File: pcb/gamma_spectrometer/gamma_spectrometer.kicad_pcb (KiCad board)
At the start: 4 copper layers, 45 x 45 mm, 184 parts, among them J101 DX07S024WJ3R400, Q201 IRLML0040, Q401 MMBTA42, Q402 MMBTA42, Q403 MMBTA42, T201 ATB322524-0110-T000, U101 LP5907MFX-3.3, U102 AMS1117-3.3, U103 FT231XQ, U104 TPS60400DBV, U201 max1847eee+, U202 TL431, U301 TL431, U302 STM32G474MET6, U303 W25Q64JVSSIQ, U401 AD8000YRDZ-REEL, Y301 ABM8G-16.000MHZ-4Y-T3

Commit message: pcb: рабочее состояние разводки USB/Power (промежуточное сохранение)
Co-Authored-By: Claude Opus 4.8 <noreply@anthropic.com>
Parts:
- C107, C109, U103: moved to B.Cu
- moved C106 73.5 mm to (113.5, 106.0)
- moved C103 72.3 mm to (111.0, 113.5)
- moved C108 71.9 mm to (113.5, 108.0)
- moved C105 71.9 mm to (112.5, 93.5), turned to 90 degrees
- moved C104 70.7 mm to (107.5, 106.5), turned to 180 degrees
- moved C107 67.3 mm to (111.9, 95.0)
- moved U102 63.1 mm to (112.0, 101.0)
- moved U101 62.5 mm to (113.5, 110.5)
- moved C101 59.0 mm to (92.5, 107.0), turned to 180 degrees
- moved C102 58.6 mm to (98.0, 105.0)
- moved C109 56.9 mm to (102.6, 92.5), turned to 180 degrees
- moved C110 55.6 mm to (98.0, 106.5)
- moved C112 55.0 mm to (92.5, 110.5), turned to 180 degrees
- moved C116 53.2 mm to (93.1, 117.0), turned to 180 degrees
- moved R101 52.9 mm to (106.5, 89.5), turned to 180 degrees
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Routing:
- net +5V_USB: track 0.00 -> 33.1 mm
- net +3.3V_D: track 0.00 -> 30.4 mm, vias 0 -> 2
- net Net-(F101-Pad1): track 0.00 -> 22.1 mm, vias 0 -> 2
- net +5V_A: track 0.00 -> 15.8 mm
- net /USB_Power_Board/D_N: track 0.00 -> 14.7 mm, vias 0 -> 3
- net GND: track 0.00 -> 13.7 mm, vias 0 -> 41
- net /USB_Power_Board/D_P: track 0.00 -> 11.9 mm, vias 0 -> 1
- net Net-(U104-OUT): track 0.00 -> 8.32 mm
- net Net-(U104-C_{FLY+}): track 0.00 -> 7.31 mm
- net −5V_A: track 0.00 -> 6.64 mm
- net +5V_HV: track 0.00 -> 5.53 mm
- net Net-(J101-PadB5): track 0.00 -> 4.36 mm
- net +3.3V_A: track 0.00 -> 3.74 mm
- net Net-(J101-PadA5): track 0.00 -> 3.09 mm
- net Net-(U103-CBUS0): track 0.00 -> 2.81 mm, vias 0 -> 1
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- added copper zone on B.Cu, net GND
- added copper zone on F.Cu, net GND
- added copper zone on In1.Cu, net GND

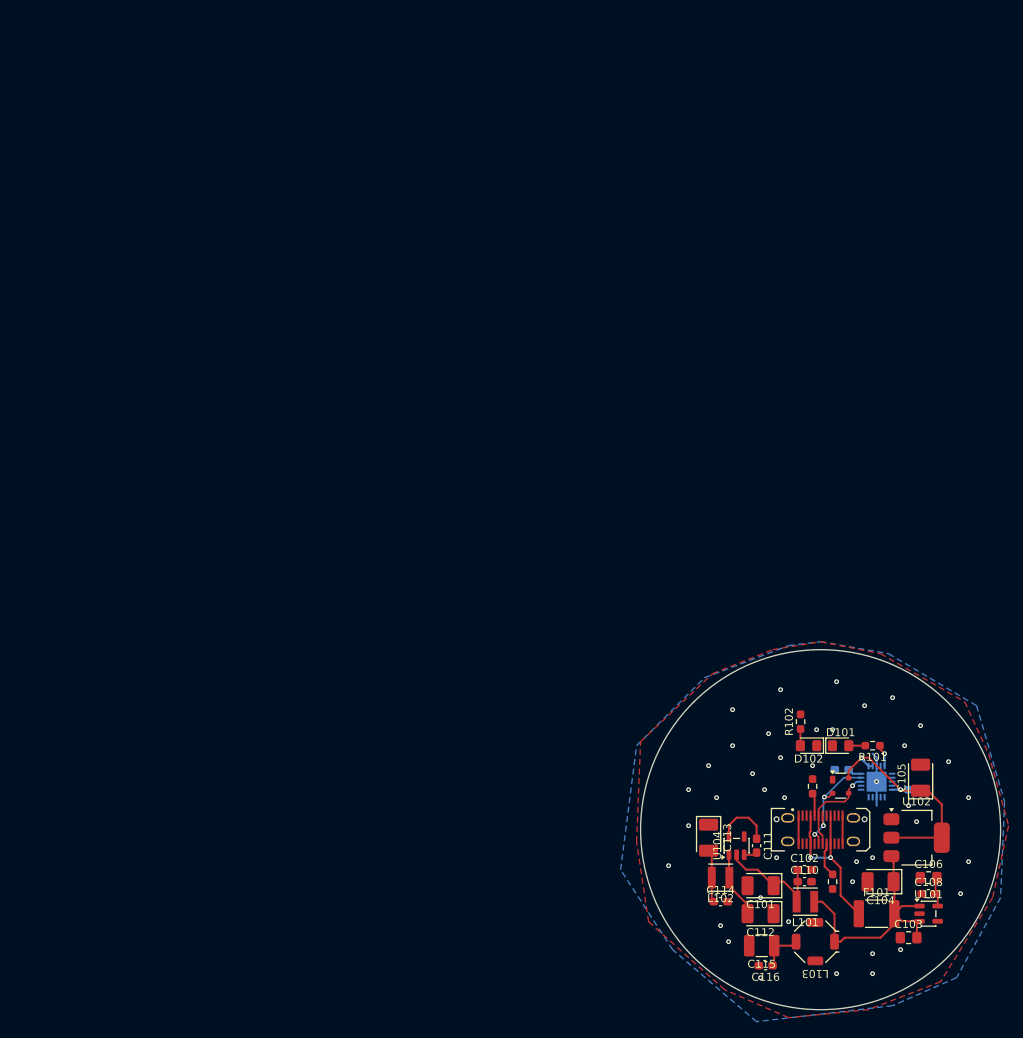
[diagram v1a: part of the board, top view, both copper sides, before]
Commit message: pcb(usb): односторонний монтаж + стойки M2.5 + своп ESD D+/D−
- FT231X (U103) + C107/C109 перенесены на верхний слой → на B.Cu
  компонентов 0, монтаж односторонний (проще/дешевле в сборке).
- U_ESD101: D+/D− переставлены на I/O1/I/O2 (пины симметричны по
  даташиту PRTR5V0U2X) ради компоновки; идентичность линий сохранена
  (D+ →USBDP, D− →USBDM). Нетлист переэкспортирован.
- Стойки M2.5 (STANDOFF_x3_TRIANGLE) в центр (100,100), все 3 пэда на GND.
- docs: usb_power_board_schematic синхронизирован (D+/D− таблица,
  корпус SOT143B вместо ошибочного SOT-363); добавлен даташит PRTR5V0U2X.

Co-Authored-By: Claude Opus 4.8 <noreply@anthropic.com>
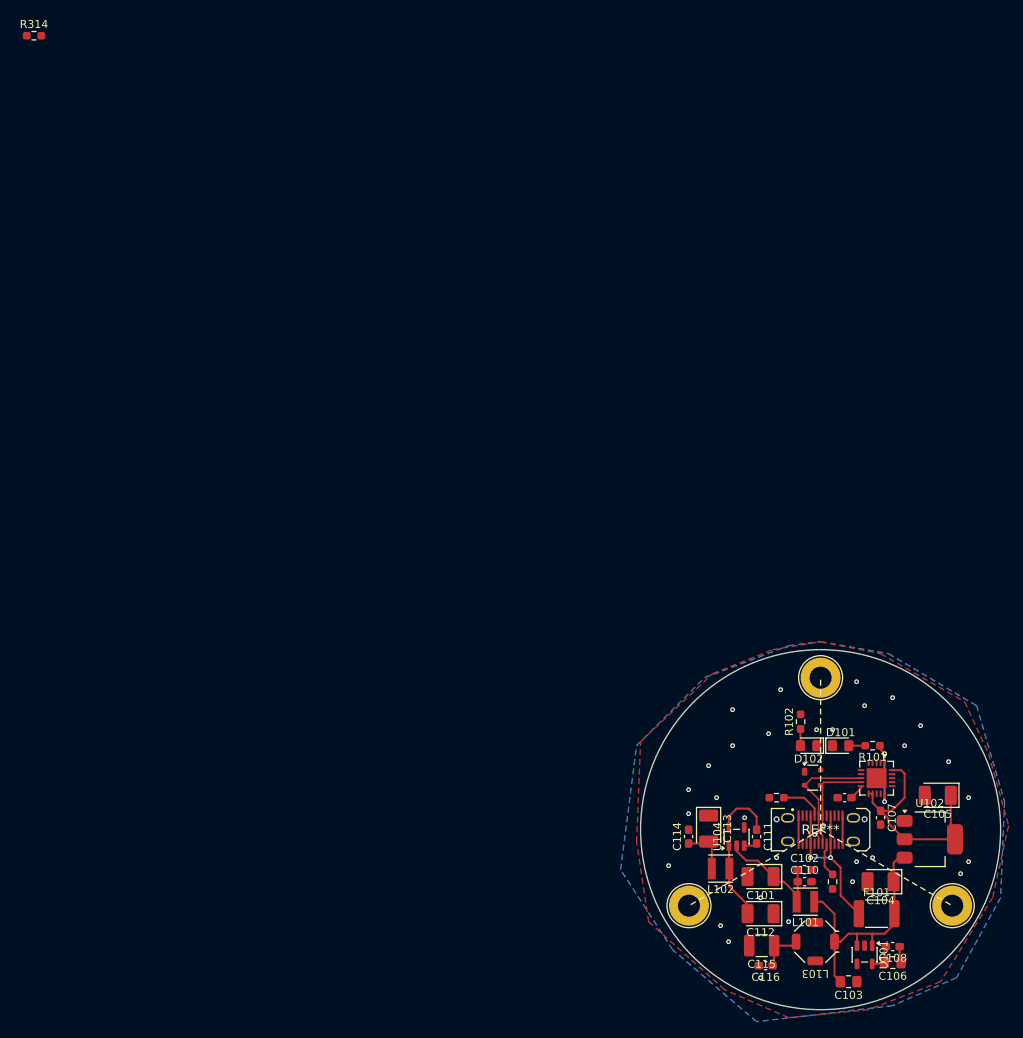
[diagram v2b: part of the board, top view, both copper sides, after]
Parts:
- added R314: 10k, Resistor_SMD:R_0603_1608Metric_Pad0.98x0.95mm_HandSolder, F.Cu at (1.68, 0.76)
- added REF**: STANDOFF_M2.5_GND_x3_TRIANGLE, посадочные места:STANDOFF_M2.5_GND_x3_TRIANGLE, F.Cu at (100.0, 100.0)
- C107, C109, U103: moved to F.Cu
- R412: value 499k -> 1M
- moved C106 11.5 mm to (109.0, 116.6), turned to 180 degrees
- moved U101 9.51 mm to (105.5, 115.6), turned to -90 degrees
- moved C103 9.30 mm to (103.5, 119.0), turned to 180 degrees
- moved C114 9.07 mm to (83.5, 100.9), turned to 90 degrees
- moved C108 7.99 mm to (109.0, 114.6), turned to 180 degrees
- moved C107 5.59 mm to (107.5, 98.5), turned to -90 degrees
- moved R_CC102 4.72 mm to (94.5, 96.0), turned to 180 degrees
- moved U_ESD101 3.64 mm to (99.0, 93.5)
- moved C109 3.52 mm to (103.0, 96.0)
- moved C105 3.08 mm to (114.7, 95.7), turned to 180 degrees
- moved U102 1.66 mm to (113.7, 101.2)
- moved C101 1.14 mm to (92.5, 105.9)
- moved C111 1.14 mm to (92.0, 100.9)
- moved C113 1.14 mm to (86.0, 99.9)
- moved L102 1.14 mm to (87.5, 104.9)
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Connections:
- Q403 pad 3: Net-(Q403-C) -> GND
- R412 pad 2: Net-(Q403-C) -> GND
- U_ESD101 pad 2: /USB_Power_Board/D_N -> /USB_Power_Board/D_P
- U_ESD101 pad 3: /USB_Power_Board/D_P -> /USB_Power_Board/D_N
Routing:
- net Net-(U103-CBUS0): track 2.81 -> 7.83 mm, vias 1 -> 2
- net GND: track 13.7 -> 9.07 mm, vias 41 -> 30
- net /USB_Power_Board/D_P: track 11.9 -> 15.7 mm, vias 1 -> 0
- net Net-(J101-PadA5): track 3.09 -> 5.32 mm
- net +3.3V_D: track 30.4 -> 28.3 mm, vias 2 -> 0
- net /USB_Power_Board/D_N: track 14.7 -> 13.4 mm, vias 3 -> 2
- net Net-(U104-OUT): track 8.32 -> 9.46 mm
- net −5V_A: track 6.64 -> 6.14 mm

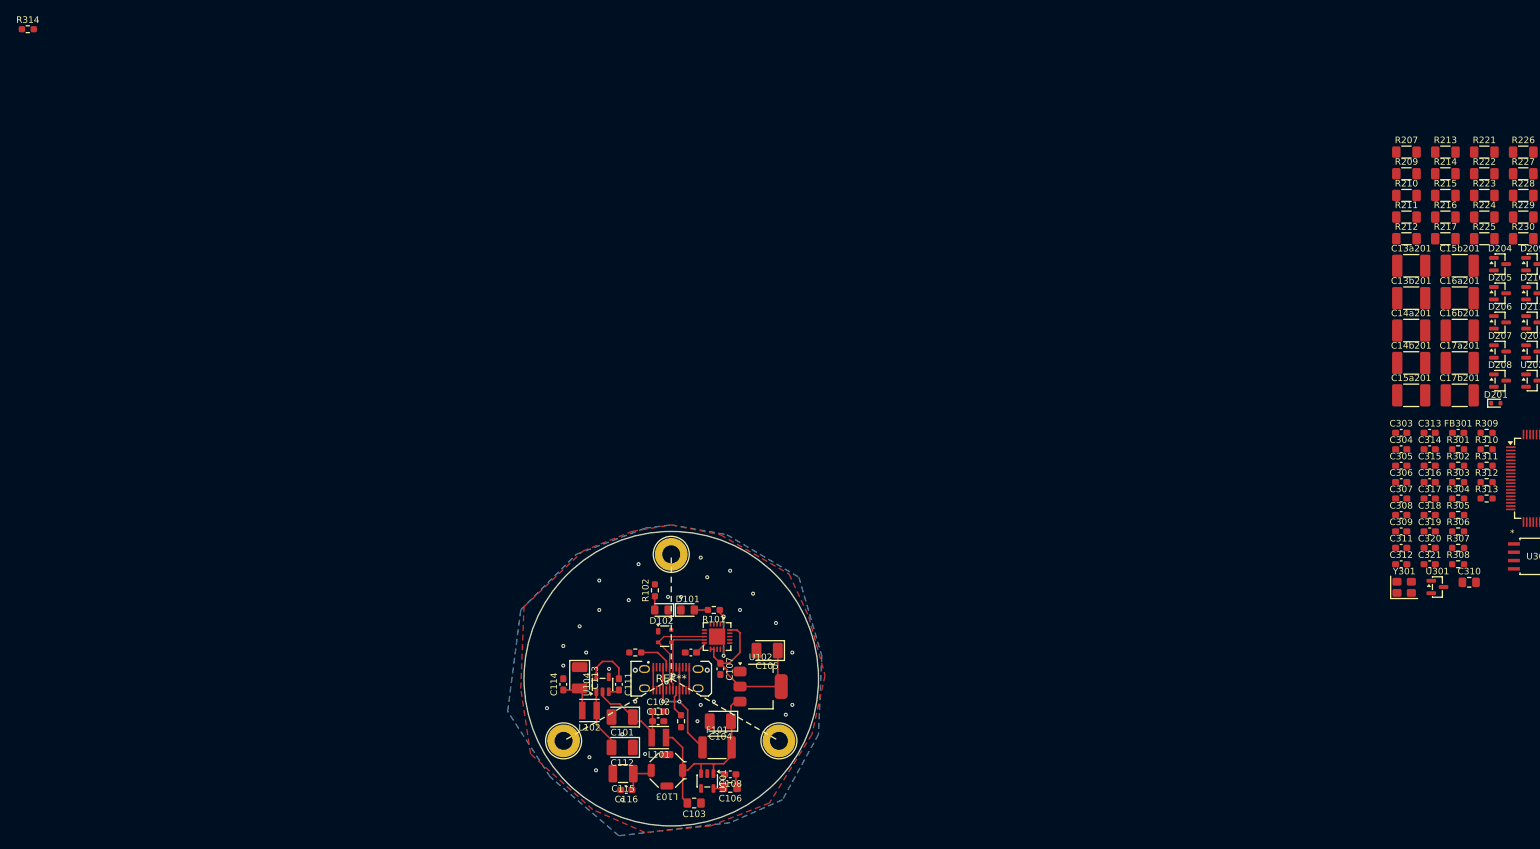
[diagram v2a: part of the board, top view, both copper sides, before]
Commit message: pcb(usb): GND-сшивка вианами + фикс C106/U101 + ESD VCC — DRC чист
- Земля сшита вианами F.Cu/In1.Cu/B.Cu (виасы у U103, R_CC101, C109);
  GND-полигон собран в единый, островов нет.
- Устранено наложение courtyard C106 ↔ U101.
- U_ESD101 пин 4 (+3.3V_D) подключён.
- DRC (headless kicad-cli): USB-локальных неподключённых 0, электрических
  нарушений 0. Остаётся косметика silk (44) и кросс-плата (ждёт межплатных пинов).

Co-Authored-By: Claude Opus 4.8 <noreply@anthropic.com>
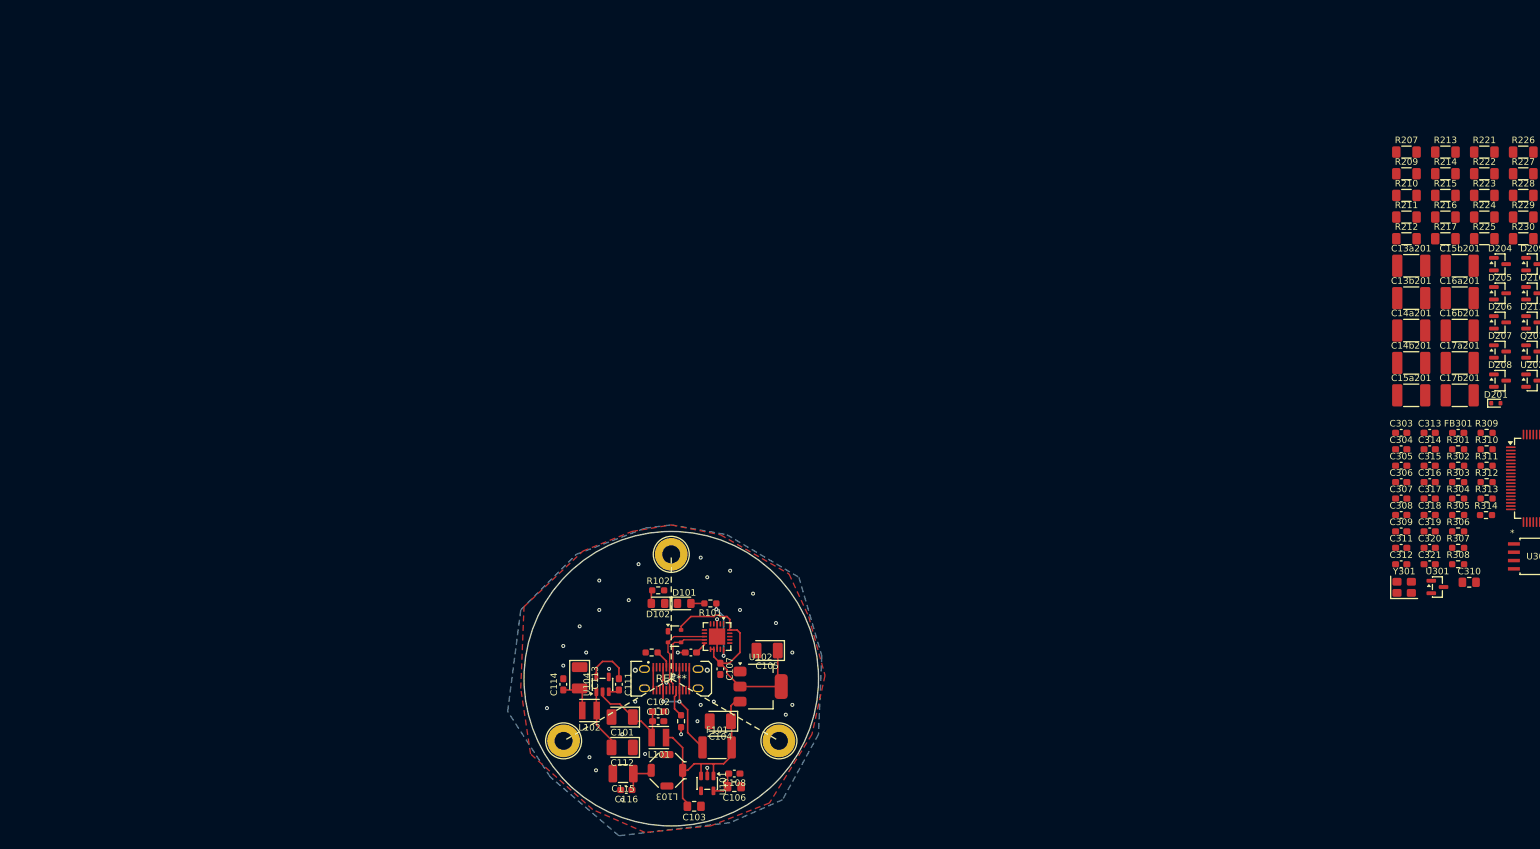
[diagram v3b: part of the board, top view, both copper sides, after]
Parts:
- moved R314 234.9 mm to (224.5, 75.0)
- moved R_CC102 2.50 mm to (97.0, 96.0)
- moved U_ESD101 1.50 mm to (100.5, 93.5)
- moved D101 1.13 mm to (102.0, 88.5)
- moved D102 1.13 mm to (98.0, 88.5)
- moved R101 1.13 mm to (106.0, 88.5)
- moved C106 0.63 mm to (109.6, 116.5)
- moved C108 0.63 mm to (109.6, 114.5)
- moved C103 0.50 mm to (103.5, 119.5)
- moved R102 0.50 mm to (98.0, 86.5), turned to 0 degrees
- moved U101 0.36 mm to (105.5, 116.0)
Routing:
- net +3.3V_D: track 28.3 -> 38.9 mm
- net GND: track 9.07 -> 15.0 mm, vias 30 -> 32
- net Net-(J101-PadA5): track 5.32 -> 2.82 mm
- net /USB_Power_Board/D_P: track 15.7 -> 13.5 mm
- net Net-(U103-CBUS0): track 7.83 -> 9.46 mm
- net +5V_USB: track 33.0 -> 34.2 mm
- net /USB_Power_Board/D_N: track 13.4 -> 12.9 mm
